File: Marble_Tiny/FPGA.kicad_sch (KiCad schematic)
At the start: 43 parts, among them T1 BSS138LT1G, T2 BSS138LT1G, U1 XC7A35T-CSG325, U28 24AA256UID-I_ST

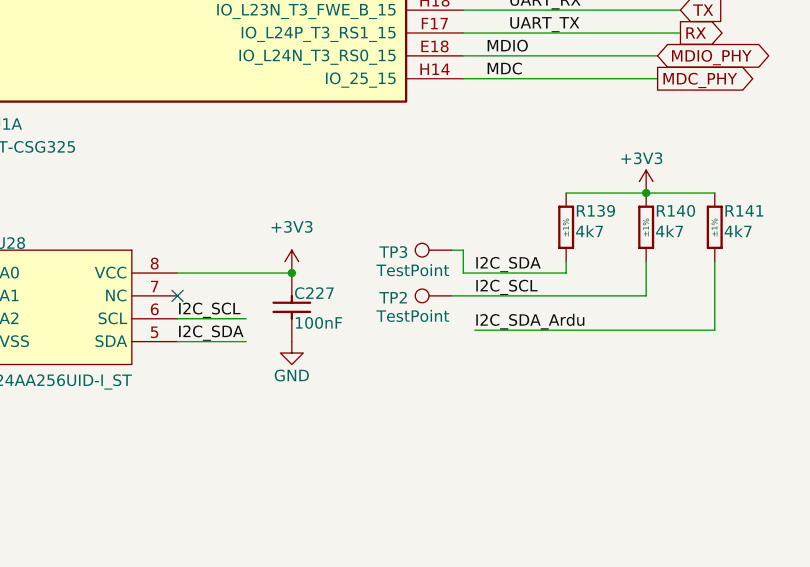
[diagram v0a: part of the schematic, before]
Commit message: fixed ERCs; added test points; added WP switch
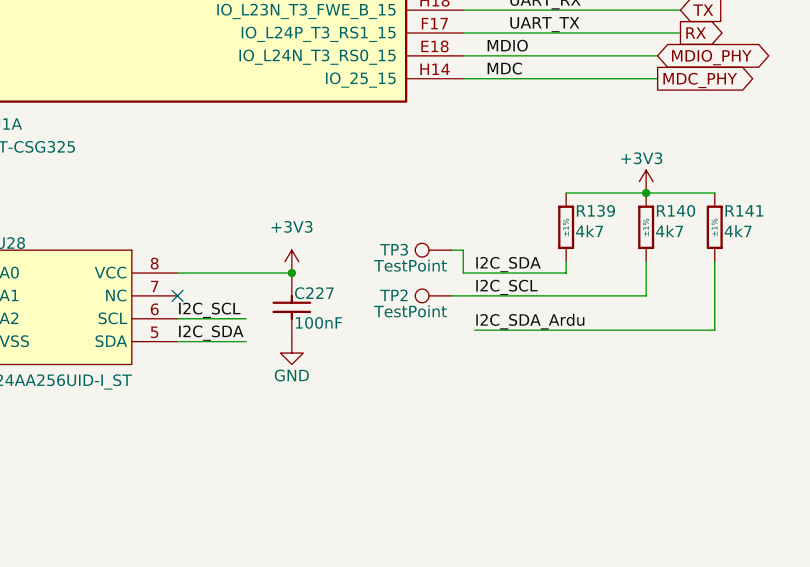
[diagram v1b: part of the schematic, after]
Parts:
- removed TP2, TP3: TestPoint, TestPoint:TestPoint_THTPad_D1.5mm_Drill0.7mm, symbol Connector_Generic:TestPoint
- added TP2, TP3: TestPoint, TestPoint:TestPoint_Pad_D1.5mm, symbol Connector:TestPoint
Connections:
- net I2C_SCL: now also TP2.1
- net I2C_SDA: now also TP3.1
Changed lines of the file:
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@@
 	)
 	(symbol
+		(lib_id "Connector:TestPoint")
+		(at 190.5 234.95 90)
+		(unit 1)
+		(exclude_from_sim no)
+		(in_bom yes)
+		(on_board yes)
+		(dnp no)
+		(property "Reference" "TP2"
+			(at 184.15 234.95 90)
+			(effects
+				(font
+					(size 1.27 1.27)
+				)
+			)
+		)
+		(property "Value" "TestPoint"
+			(at 185.928 236.728 90)
+			(effects
+				(font
+					(size 1.27 1.27)
+				)
+			)
+		)
+		(property "Footprint" "TestPoint:TestPoint_Pad_D1.5mm"
+			(at 190.5 229.87 0)
+			(effects
+				(font
+					(size 1.27 1.27)
+				)
+				(hide yes)
+			)
+		)
+		(property "Datasheet" "~"
+			(at 190.5 229.87 0)
+			(effects
+				(font
+					(size 1.27 1.27)
+				)
+				(hide yes)
+			)
+		)
+		(property "Description" "test point"
+			(at 190.5 234.95 0)
+			(effects
+				(font
+					(size 1.27 1.27)
+				)
+				(hide yes)
+			)
+		)
+		(pin "1"
+		)
+		(instances
+			(project "Marble_Tiny"
+				(path "/c2a4f786-b14c-434a-acf7-b20fb2221b0b/26bc6f09-ebb0-4c32-8a32-ec70c3f97c4f"
+					(reference "TP2")
+					(unit 1)
+				)
+			)
+		)
+	)
+	(symbol
 		(lib_id "LEDs & Displays:LED_KINGBRIGHT_KPH-1608CGCK")
 		(at 242.57 241.3 270)
@@
 	)
 	(symbol
-		(lib_id "Connector_Generic:TestPoint")
-		(at 190.5 234.95 90)
-		(mirror x)
-		(unit 1)
-		(exclude_from_sim no)
-		(in_bom yes)
-		(on_board yes)
-		(dnp no)
-		(property "Reference" "TP2"
-			(at 185.674 235.204 90)
-			(effects
-				(font
-					(size 1.27 1.27)
-				)
-				(justify left)
-			)
-		)
-		(property "Value" "TestPoint"
-			(at 190.246 237.236 90)
-			(effects
-				(font
-					(size 1.27 1.27)
-				)
-				(justify left)
-			)
-		)
-		(property "Footprint" "TestPoint:TestPoint_THTPad_D1.5mm_Drill0.7mm"
-			(at 190.5 240.03 0)
-			(effects
-				(font
-					(size 1.27 1.27)
-				)
-				(hide yes)
-			)
-		)
-		(property "Datasheet" ""
-			(at 190.5 240.03 0)
-			(effects
-				(font
-					(size 1.27 1.27)
-				)
-				(hide yes)
-			)
-		)
-		(property "Description" ""
-			(at 190.5 234.95 0)
-			(effects
-				(font
-					(size 1.27 1.27)
-				)
-				(hide yes)
-			)
-		)
-		(pin "1"
-		)
-		(instances
-			(project "Marble_Tiny"
-				(path "/c2a4f786-b14c-434a-acf7-b20fb2221b0b/26bc6f09-ebb0-4c32-8a32-ec70c3f97c4f"
-					(reference "TP2")
-					(unit 1)
-				)
-			)
-		)
-	)
-	(symbol
 		(lib_id "Capacitors SMD:CC0201_470NF_4V_20%_X5R")
 		(at 88.9 59.69 90)
@@
 	)
 	(symbol
+		(lib_id "Connector:TestPoint")
+		(at 190.5 229.87 90)
+		(unit 1)
+		(exclude_from_sim no)
+		(in_bom yes)
+		(on_board yes)
+		(dnp no)
+		(property "Reference" "TP3"
+			(at 184.15 229.87 90)
+			(effects
+				(font
+					(size 1.27 1.27)
+				)
+			)
+		)
+		(property "Value" "TestPoint"
+			(at 185.928 231.648 90)
+			(effects
+				(font
+					(size 1.27 1.27)
+				)
+			)
+		)
+		(property "Footprint" "TestPoint:TestPoint_Pad_D1.5mm"
+			(at 190.5 224.79 0)
+			(effects
+				(font
+					(size 1.27 1.27)
+				)
+				(hide yes)
+			)
+		)
+		(property "Datasheet" "~"
+			(at 190.5 224.79 0)
+			(effects
+				(font
+					(size 1.27 1.27)
+				)
+				(hide yes)
+			)
+		)
+		(property "Description" "test point"
+			(at 190.5 229.87 0)
+			(effects
+				(font
+					(size 1.27 1.27)
+				)
+				(hide yes)
+			)
+		)
+		(pin "1"
+		)
+		(instances
+			(project "Marble_Tiny"
+				(path "/c2a4f786-b14c-434a-acf7-b20fb2221b0b/26bc6f09-ebb0-4c32-8a32-ec70c3f97c4f"
+					(reference "TP3")
+					(unit 1)
+				)
+			)
+		)
+	)
+	(symbol
 		(lib_id "Resistors SMD:R0402_4K7_1%_0.0625W_100PPM")
 		(at 203.2 231.14 90)
@@
 					(unit 1)
 				)
-			)
-		)
-	)
-	(symbol
-		(lib_id "Connector_Generic:TestPoint")
-		(at 190.5 229.87 90)
-		(mirror x)
-		(unit 1)
-		(exclude_from_sim no)
-		(in_bom yes)
-		(on_board yes)
-		(dnp no)
-		(property "Reference" "TP3"
-			(at 185.674 230.124 90)
-			(effects
-				(font
-					(size 1.27 1.27)
-				)
-				(justify left)
-			)
-		)
-		(property "Value" "TestPoint"
-			(at 190.246 232.156 90)
-			(effects
-				(font
-					(size 1.27 1.27)
-				)
-				(justify left)
-			)
-		)
-		(property "Footprint" "TestPoint:TestPoint_THTPad_D1.5mm_Drill0.7mm"
-			(at 190.5 234.95 0)
-			(effects
-				(font
-					(size 1.27 1.27)
-				)
-				(hide yes)
-			)
-		)
-		(property "Datasheet" ""
-			(at 190.5 234.95 0)
-			(effects
-				(font
-					(size 1.27 1.27)
-				)
-				(hide yes)
-			)
-		)
-		(property "Description" ""
-			(at 190.5 229.87 0)
-			(effects
-				(font
-					(size 1.27 1.27)
-				)
-				(hide yes)
-			)
-		)
-		(pin "1"
-		)
-		(instances
-			(project "Marble_Tiny"
-				(path "/c2a4f786-b14c-434a-acf7-b20fb2221b0b/26bc6f09-ebb0-4c32-8a32-ec70c3f97c4f"
-					(reference "TP3")
-					(unit 1)
-				)

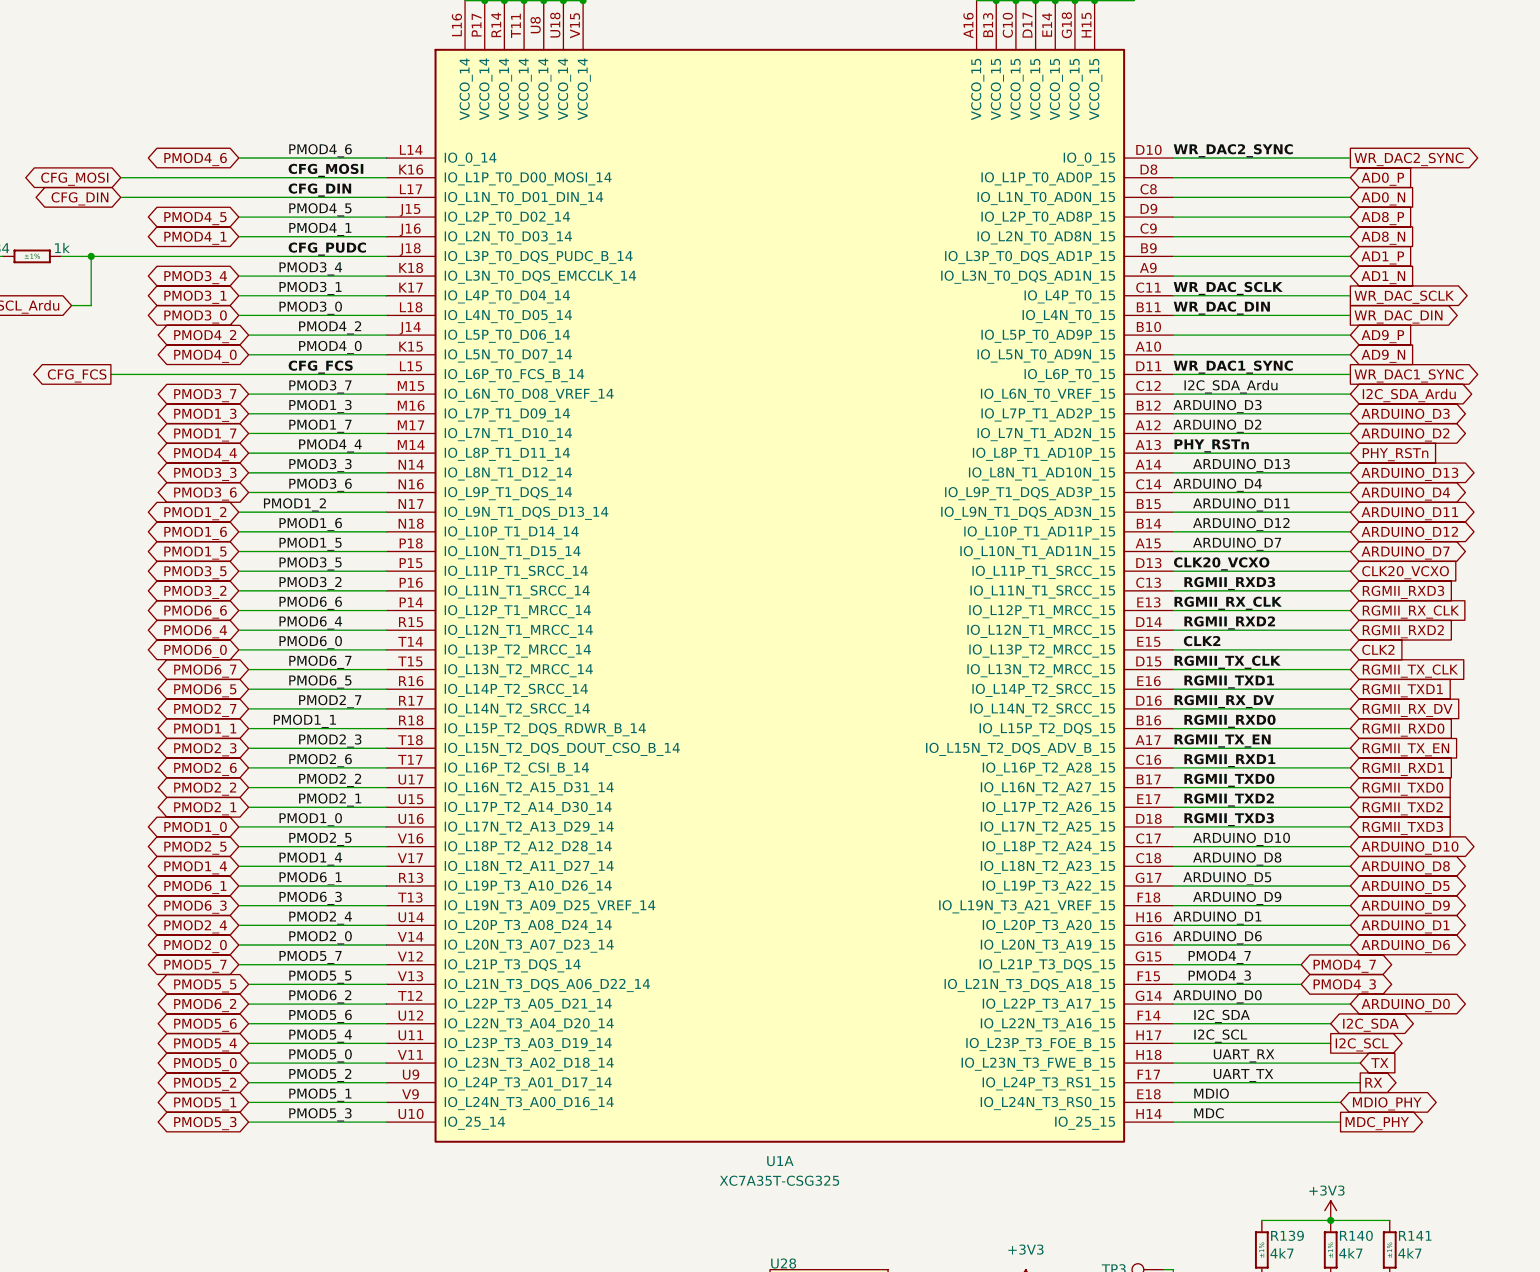
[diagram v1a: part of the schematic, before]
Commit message: fixed issue with PMODs; added board name and revision; fixed polygons issue
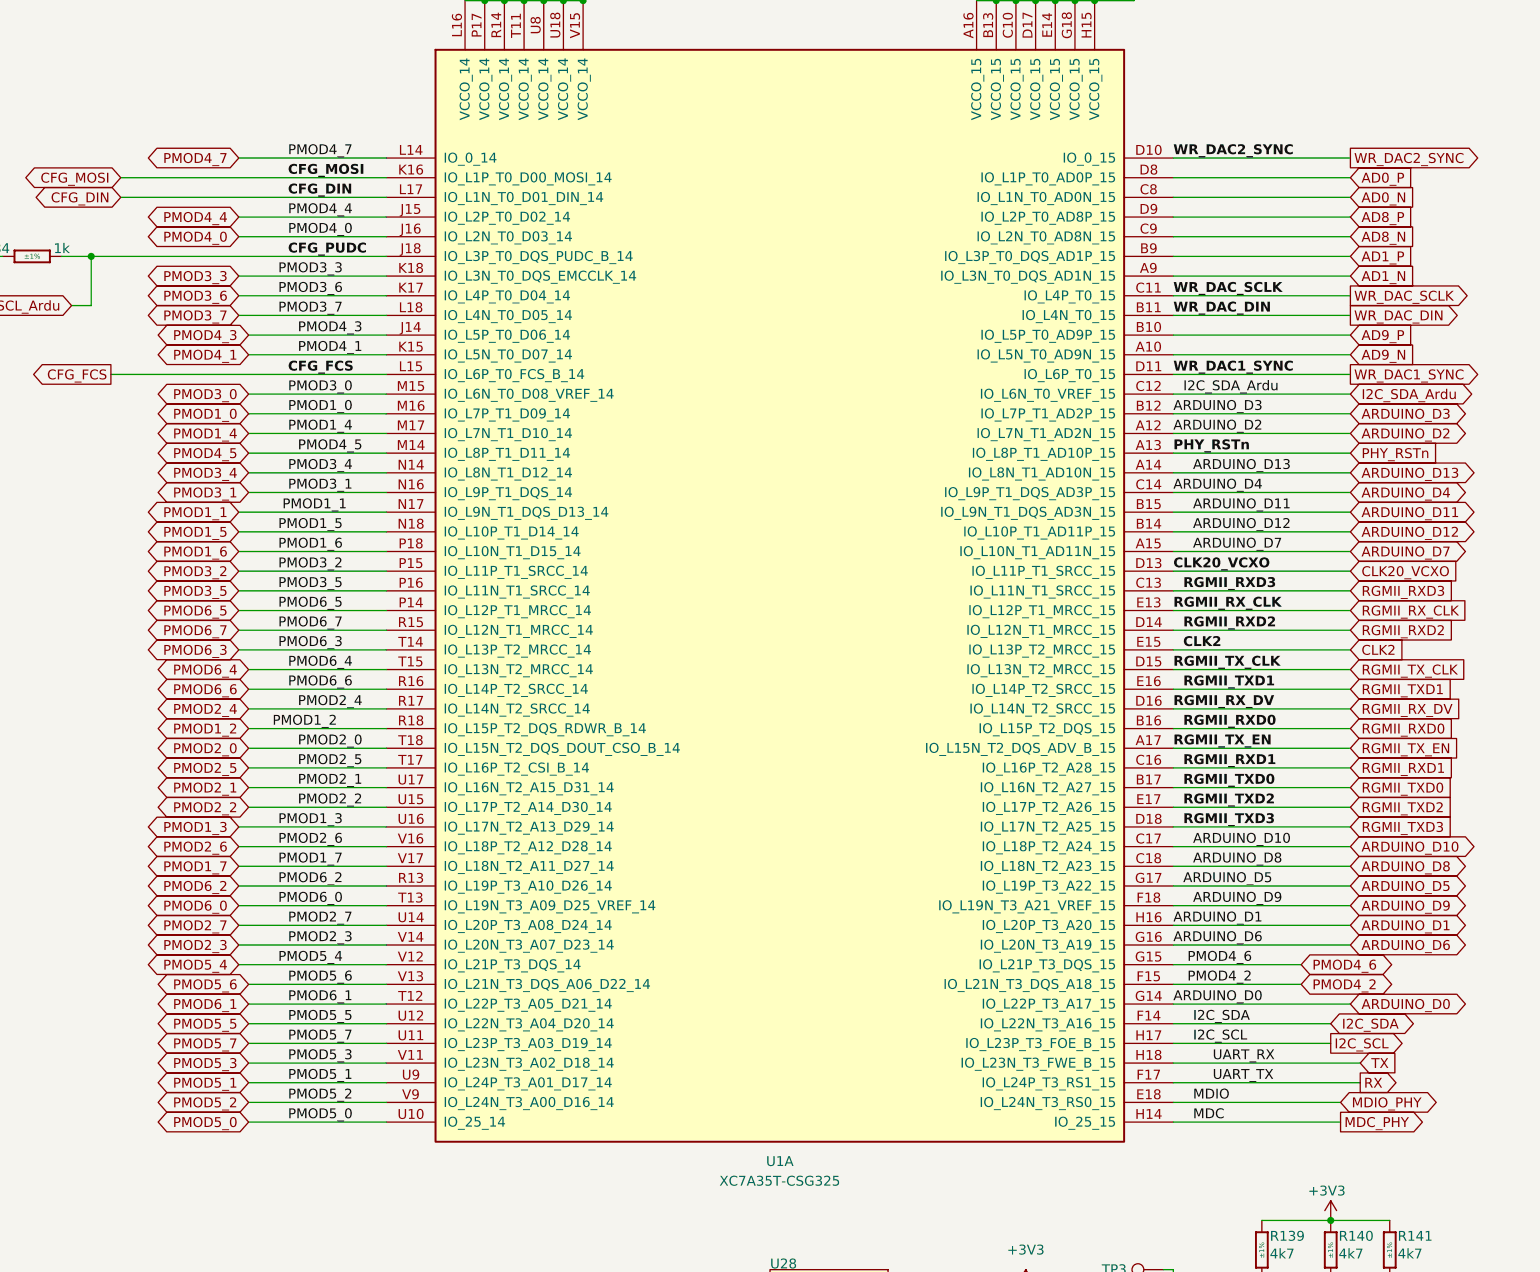
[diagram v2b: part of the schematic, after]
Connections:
- net PMOD1_0: now also U1.M16 (IO_L7P_T1_D09_14); no longer U1.U16 (IO_L17N_T2_A13_D29_14)
- net PMOD1_1: now also U1.N17 (IO_L9N_T1_DQS_D13_14); no longer U1.R18 (IO_L15P_T2_DQS_RDWR_B_14)
- net PMOD1_2: now also U1.R18 (IO_L15P_T2_DQS_RDWR_B_14); no longer U1.N17 (IO_L9N_T1_DQS_D13_14)
- net PMOD1_3: now also U1.U16 (IO_L17N_T2_A13_D29_14); no longer U1.M16 (IO_L7P_T1_D09_14)
- net PMOD1_4: now also U1.M17 (IO_L7N_T1_D10_14); no longer U1.V17 (IO_L18N_T2_A11_D27_14)
- net PMOD1_5: now also U1.N18 (IO_L10P_T1_D14_14); no longer U1.P18 (IO_L10N_T1_D15_14)
- net PMOD1_6: now also U1.P18 (IO_L10N_T1_D15_14); no longer U1.N18 (IO_L10P_T1_D14_14)
- net PMOD1_7: now also U1.V17 (IO_L18N_T2_A11_D27_14); no longer U1.M17 (IO_L7N_T1_D10_14)
- net PMOD2_0: now also U1.T18 (IO_L15N_T2_DQS_DOUT_CSO_B_14); no longer U1.V14 (IO_L20N_T3_A07_D23_14)
- net PMOD2_1: now also U1.U17 (IO_L16N_T2_A15_D31_14); no longer U1.U15 (IO_L17P_T2_A14_D30_14)
- net PMOD2_2: now also U1.U15 (IO_L17P_T2_A14_D30_14); no longer U1.U17 (IO_L16N_T2_A15_D31_14)
- net PMOD2_3: now also U1.V14 (IO_L20N_T3_A07_D23_14); no longer U1.T18 (IO_L15N_T2_DQS_DOUT_CSO_B_14)
- net PMOD2_4: now also U1.R17 (IO_L14N_T2_SRCC_14); no longer U1.U14 (IO_L20P_T3_A08_D24_14)
- net PMOD2_5: now also U1.T17 (IO_L16P_T2_CSI_B_14); no longer U1.V16 (IO_L18P_T2_A12_D28_14)
- net PMOD2_6: now also U1.V16 (IO_L18P_T2_A12_D28_14); no longer U1.T17 (IO_L16P_T2_CSI_B_14)
- net PMOD2_7: now also U1.U14 (IO_L20P_T3_A08_D24_14); no longer U1.R17 (IO_L14N_T2_SRCC_14)
- net PMOD3_0: now also U1.M15 (IO_L6N_T0_D08_VREF_14); no longer U1.L18 (IO_L4N_T0_D05_14)
- net PMOD3_1: now also U1.N16 (IO_L9P_T1_DQS_14); no longer U1.K17 (IO_L4P_T0_D04_14)
- net PMOD3_2: now also U1.P15 (IO_L11P_T1_SRCC_14); no longer U1.P16 (IO_L11N_T1_SRCC_14)
- net PMOD3_3: now also U1.K18 (IO_L3N_T0_DQS_EMCCLK_14); no longer U1.N14 (IO_L8N_T1_D12_14)
- net PMOD3_4: now also U1.N14 (IO_L8N_T1_D12_14); no longer U1.K18 (IO_L3N_T0_DQS_EMCCLK_14)
- net PMOD3_5: now also U1.P16 (IO_L11N_T1_SRCC_14); no longer U1.P15 (IO_L11P_T1_SRCC_14)
- net PMOD3_6: now also U1.K17 (IO_L4P_T0_D04_14); no longer U1.N16 (IO_L9P_T1_DQS_14)
- net PMOD3_7: now also U1.L18 (IO_L4N_T0_D05_14); no longer U1.M15 (IO_L6N_T0_D08_VREF_14)
- net PMOD4_0: now also U1.J16 (IO_L2N_T0_D03_14); no longer U1.K15 (IO_L5N_T0_D07_14)
- net PMOD4_1: now also U1.K15 (IO_L5N_T0_D07_14); no longer U1.J16 (IO_L2N_T0_D03_14)
- net PMOD4_2: now also U1.F15 (IO_L21N_T3_DQS_A18_15); no longer U1.J14 (IO_L5P_T0_D06_14)
- net PMOD4_3: now also U1.J14 (IO_L5P_T0_D06_14); no longer U1.F15 (IO_L21N_T3_DQS_A18_15)
- net PMOD4_4: now also U1.J15 (IO_L2P_T0_D02_14); no longer U1.M14 (IO_L8P_T1_D11_14)
- net PMOD4_5: now also U1.M14 (IO_L8P_T1_D11_14); no longer U1.J15 (IO_L2P_T0_D02_14)
- net PMOD4_6: now also U1.G15 (IO_L21P_T3_DQS_15); no longer U1.L14 (IO_0_14)
- net PMOD4_7: now also U1.L14 (IO_0_14); no longer U1.G15 (IO_L21P_T3_DQS_15)
- net PMOD5_0: now also U1.U10 (IO_25_14); no longer U1.V11 (IO_L23N_T3_A02_D18_14)
- net PMOD5_1: now also U1.U9 (IO_L24P_T3_A01_D17_14); no longer U1.V9 (IO_L24N_T3_A00_D16_14)
- net PMOD5_2: now also U1.V9 (IO_L24N_T3_A00_D16_14); no longer U1.U9 (IO_L24P_T3_A01_D17_14)
- net PMOD5_3: now also U1.V11 (IO_L23N_T3_A02_D18_14); no longer U1.U10 (IO_25_14)
- net PMOD5_4: now also U1.V12 (IO_L21P_T3_DQS_14); no longer U1.U11 (IO_L23P_T3_A03_D19_14)
- net PMOD5_5: now also U1.U12 (IO_L22N_T3_A04_D20_14); no longer U1.V13 (IO_L21N_T3_DQS_A06_D22_14)
- net PMOD5_6: now also U1.V13 (IO_L21N_T3_DQS_A06_D22_14); no longer U1.U12 (IO_L22N_T3_A04_D20_14)
- net PMOD5_7: now also U1.U11 (IO_L23P_T3_A03_D19_14); no longer U1.V12 (IO_L21P_T3_DQS_14)
- net PMOD6_0: now also U1.T13 (IO_L19N_T3_A09_D25_VREF_14); no longer U1.T14 (IO_L13P_T2_MRCC_14)
- net PMOD6_1: now also U1.T12 (IO_L22P_T3_A05_D21_14); no longer U1.R13 (IO_L19P_T3_A10_D26_14)
- net PMOD6_2: now also U1.R13 (IO_L19P_T3_A10_D26_14); no longer U1.T12 (IO_L22P_T3_A05_D21_14)
- net PMOD6_3: now also U1.T14 (IO_L13P_T2_MRCC_14); no longer U1.T13 (IO_L19N_T3_A09_D25_VREF_14)
- net PMOD6_4: now also U1.T15 (IO_L13N_T2_MRCC_14); no longer U1.R15 (IO_L12N_T1_MRCC_14)
- net PMOD6_5: now also U1.P14 (IO_L12P_T1_MRCC_14); no longer U1.R16 (IO_L14P_T2_SRCC_14)
- net PMOD6_6: now also U1.R16 (IO_L14P_T2_SRCC_14); no longer U1.P14 (IO_L12P_T1_MRCC_14)
- net PMOD6_7: now also U1.R15 (IO_L12N_T1_MRCC_14); no longer U1.T15 (IO_L13N_T2_MRCC_14)
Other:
- company: (none) -> ${name}
